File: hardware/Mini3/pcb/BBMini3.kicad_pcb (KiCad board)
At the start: 4 copper layers, 88 x 50 mm, 79 parts, among them J1 Conn_01x02, J2 USB_B_Mini, Q1 MBT2222ADW1T1, SW1 SW_SPDT, SW2 SW_Push, SW3 SW_Push, SW4 SW_Push, U1 ESP8266EX, U2 AT25SF081-SSHF-X, U3 AP2112K-3.3, U4 CP2104, U5 MCP3208, U6 LM2576S-5, U7 HD44780, U8 74HC595, Y1 ABM8-26.000MHZ-10-1-U-T

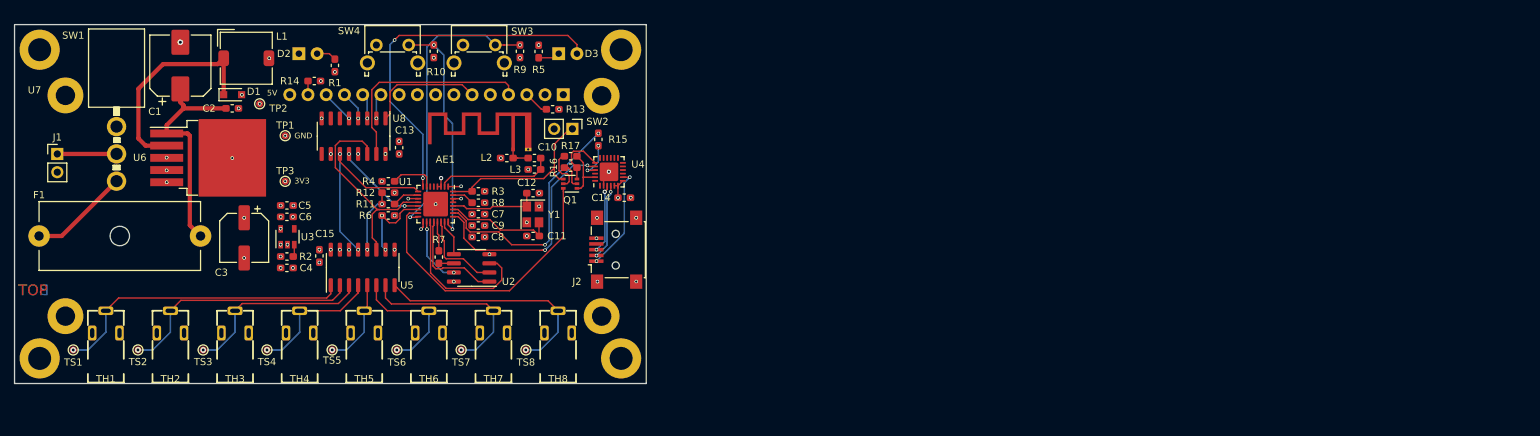
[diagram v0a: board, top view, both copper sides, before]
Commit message: feat: Version 3: Experimental PCB with only one ADC and multiplexer
shrink stuff, start pcb

Issue #24
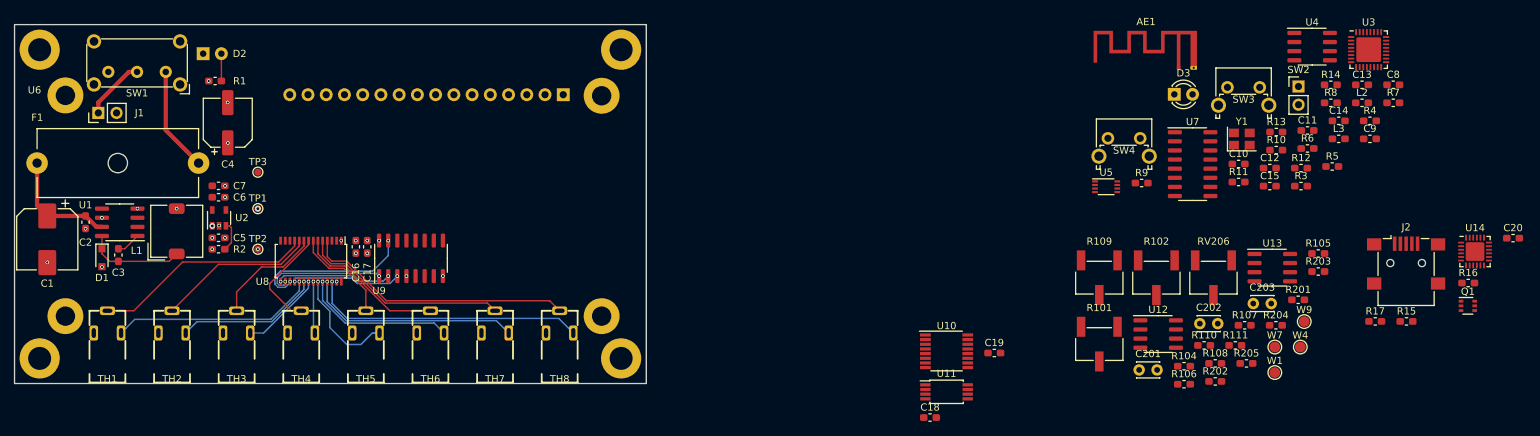
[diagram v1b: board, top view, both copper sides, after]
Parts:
- removed TS1, TS2, TS3, TS4, TS5, TS6, TS7, TS8: TestPoint, TestPoint:TestPoint_Pad_D1.0mm
- removed the U6 at (42.0, 33.6)
- added C16: 100n, Capacitor_SMD:C_0603_1608Metric_Pad1.05x0.95mm_HandSolder, F.Cu at (62.5, 46.0)
- added C17: 100n, Capacitor_SMD:C_0603_1608Metric_Pad1.05x0.95mm_HandSolder, F.Cu at (64.1, 46.0)
- added C18: 100n, Capacitor_SMD:C_0603_1608Metric_Pad1.05x0.95mm_HandSolder, F.Cu at (142.5, 69.7)
- added C19: 100n, Capacitor_SMD:C_0603_1608Metric_Pad1.05x0.95mm_HandSolder, F.Cu at (151.5, 60.7)
- added C20: 100n, Capacitor_SMD:C_0603_1608Metric_Pad1.05x0.95mm_HandSolder, F.Cu at (223.8, 44.7)
- added C201: 100n, Capacitor_THT:C_Disc_D3.0mm_W2.0mm_P2.50mm, F.Cu at (171.7, 63.1)
- added C202: 100n, Capacitor_THT:C_Disc_D3.0mm_W2.0mm_P2.50mm, F.Cu at (180.1, 56.7)
- added C203: 100n, Capacitor_THT:C_Disc_D3.0mm_W2.0mm_P2.50mm, F.Cu at (187.6, 53.9)
- added R101: 405, Potentiometer_SMD:Potentiometer_Bourns_3269W_Vertical, F.Cu at (166.1, 59.5)
- added R102: 300, Potentiometer_SMD:Potentiometer_Bourns_3269W_Vertical, F.Cu at (174.1, 50.3)
- added R104: 2k2, Resistor_SMD:R_0603_1608Metric_Pad1.05x0.95mm_HandSolder, F.Cu at (177.9, 62.6)
- added R105: 10k, Resistor_SMD:R_0603_1608Metric_Pad1.05x0.95mm_HandSolder, F.Cu at (196.6, 46.9)
- added R106: 10k, Resistor_SMD:R_0603_1608Metric_Pad1.05x0.95mm_HandSolder, F.Cu at (177.9, 65.1)
- added R107: 4k7, Resistor_SMD:R_0603_1608Metric_Pad1.05x0.95mm_HandSolder, F.Cu at (186.4, 56.9)
- added R108: 200, Resistor_SMD:R_0603_1608Metric_Pad1.05x0.95mm_HandSolder, F.Cu at (182.3, 62.2)
- added R109: 470, Potentiometer_SMD:Potentiometer_Bourns_3269W_Vertical, F.Cu at (166.1, 50.3)
- added R110: 200, Resistor_SMD:R_0603_1608Metric_Pad1.05x0.95mm_HandSolder, F.Cu at (180.7, 59.7)
- added R111: 2k, Resistor_SMD:R_0603_1608Metric_Pad1.05x0.95mm_HandSolder, F.Cu at (185.1, 59.7)
- added R201: 10k, Resistor_SMD:R_0603_1608Metric_Pad1.05x0.95mm_HandSolder, F.Cu at (193.8, 53.3)
- added R202: 10k, Resistor_SMD:R_0603_1608Metric_Pad1.05x0.95mm_HandSolder, F.Cu at (182.3, 64.7)
- added R203: 10k, Resistor_SMD:R_0603_1608Metric_Pad1.05x0.95mm_HandSolder, F.Cu at (196.6, 49.4)
- added R204: 100k, Resistor_SMD:R_0603_1608Metric_Pad1.05x0.95mm_HandSolder, F.Cu at (190.7, 56.9)
- added R205: 10k, Resistor_SMD:R_0603_1608Metric_Pad1.05x0.95mm_HandSolder, F.Cu at (186.6, 62.2)
- added RV206: 10k, Potentiometer_SMD:Potentiometer_Bourns_3269W_Vertical, F.Cu at (182.0, 50.3)
- added U10: ADG709, Package_SO:TSSOP-16_4.4x5mm_P0.65mm, F.Cu at (144.8, 60.5)
- added U11: MCP3202, Package_SO:TSSOP-8_4.4x3mm_P0.65mm, F.Cu at (144.8, 66.2)
- added U12: OPA2340, Package_SO:SOIC-8_3.9x4.9mm_P1.27mm, F.Cu at (174.3, 58.1)
- added U13: OPA2340, Package_SO:SOIC-8_3.9x4.9mm_P1.27mm, F.Cu at (190.2, 48.9)
- added U14: CP2104, Package_DFN_QFN:QFN-24-1EP_4x4mm_P0.5mm_EP2.6x2.6mm, F.Cu at (218.5, 46.6)
- added U7: 74HC595, Package_SO:SOIC-16_3.9x9.9mm_P1.27mm, F.Cu at (179.1, 34.4)
- added U9: 74HC595, Package_SO:SOIC-16_3.9x9.9mm_P1.27mm, F.Cu at (70.2, 47.6)
- added W1: ~, TestPoint:TestPoint_Pad_D1.5mm, F.Cu at (190.6, 63.5)
- added W4: ~, TestPoint:TestPoint_Pad_D1.5mm, F.Cu at (194.1, 59.9)
- added W7: ~, TestPoint:TestPoint_Pad_D1.5mm, F.Cu at (190.6, 59.9)
- added W9: ~, TestPoint:TestPoint_Pad_D1.5mm, F.Cu at (194.7, 56.4)
- C10: value 5p6 -> 100n
- C11: value 10p -> 5p6
- C13: value 100n -> 10p
- C3: value 100u -> 10n; footprint Capacitor_SMD:CP_Elec_6.3x5.9 -> Capacitor_SMD:C_0603_1608Metric_Pad1.05x0.95mm_HandSolder
- C4: value 10u -> 68u; footprint Capacitor_SMD:C_0603_1608Metric_Pad1.05x0.95mm_HandSolder -> Capacitor_SMD:CP_Elec_6.3x5.9
- C6: value 1u -> 10u
- C7: value 100n -> 1u
- D3: moved to F.Cu
- L1: value 100u -> 47u
- SW1: footprint Collection:MIYAMA_MS-500-B-VT -> Button_Switch_THT:SW_E-Switch_EG1224_SPDT_Angled
- U1: value ESP8266EX -> LM2672M-5.0; footprint Package_DFN_QFN:QFN-32-1EP_5x5mm_P0.5mm_EP3.45x3.45mm -> Package_SO:SOIC-8_3.9x4.9mm_P1.27mm
- U2: value AT25SF081-SSHF-X -> AP2112K-3.3; footprint Package_SO:SOIC-8_3.9x4.9mm_P1.27mm -> Package_TO_SOT_SMD:SOT-23-5
- U3: value AP2112K-3.3 -> ESP8266EX; footprint Package_TO_SOT_SMD:SOT-23-5 -> Package_DFN_QFN:QFN-32-1EP_5x5mm_P0.5mm_EP3.45x3.45mm
- U4: value CP2104 -> AT25SF081-SSHF-X; footprint Package_DFN_QFN:QFN-24-1EP_4x4mm_P0.5mm_EP2.6x2.6mm -> Package_SO:SOIC-8_3.9x4.9mm_P1.27mm
- U5: value MCP3208 -> SN74LVC1G139; footprint Package_SO:SOIC-16_3.9x9.9mm_P1.27mm -> Package_SO:VSSOP-8_2.3x2mm_P0.5mm
- U8: value 74HC595 -> ADG707; footprint Package_SO:SOIC-16_3.9x9.9mm_P1.27mm -> Package_SO:TSSOP-28_4.4x9.7mm_P0.65mm
- moved U3 152.9 mm to (203.6, 18.5), turned to 0 degrees
- moved R14 141.6 mm to (198.4, 23.4), turned to 0 degrees
- moved R4 137.0 mm to (203.8, 28.4), turned to 0 degrees
- moved R7 134.7 mm to (207.1, 25.9), turned to 0 degrees
- moved C13 134.4 mm to (202.7, 23.4), turned to 0 degrees
- moved C15 132.8 mm to (189.9, 37.5), turned to 0 degrees
- moved C8 129.2 mm to (207.1, 23.4), turned to 0 degrees
- moved R6 128.4 mm to (195.1, 32.3)
- moved R12 127.2 mm to (194.2, 35.0), turned to 0 degrees
- moved Q1 126.2 mm to (217.5, 54.2), turned to 0 degrees
- moved R16 126.1 mm to (217.5, 51.0), turned to 0 degrees
- moved C9 124.8 mm to (203.8, 30.9), turned to 0 degrees
- moved R8 119.6 mm to (198.4, 25.9)
- moved L2 119.4 mm to (202.7, 25.9), turned to 0 degrees
- moved R11 118.5 mm to (185.5, 36.9)
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- renumbered U7 to U6
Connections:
- C10 pad 1: Net-(AE1-Pad1) -> GND
- C10 pad 2: /ESP8266EX/LNA -> +3V3
- C11 pad 1: GND -> Net-(AE1-Pad1)
- C11 pad 2: /ESP8266EX/XTAL_OUT -> /ESP8266EX/LNA
- C12 pad 2: /ESP8266EX/XTAL_IN -> /ESP8266EX/XTAL_OUT
- C13 pad 1: +5V -> GND
- C13 pad 2: GND -> /ESP8266EX/XTAL_IN
- C14 pad 1: +3V3 -> +5V
- C15 pad 2: +5V -> +3V3
- C3 pad 1: +5V -> Net-(C3-Pad1)
- C3 pad 2: GND -> Net-(C3-Pad2)
- C4 pad 1: GND -> +5V
- C4 pad 2: +5V -> GND
- C5 pad 2: +3V3 -> +5V
- C7 pad 1: +3V3 -> GND
- C7 pad 2: GND -> +3V3
- C8 pad 1: GND -> +3V3
- C8 pad 2: +3V3 -> GND
- D1 pad 1: Net-(D1-Pad1) -> Net-(C3-Pad1)
- L1 pad 1: Net-(D1-Pad1) -> Net-(C3-Pad1)
- R6 pad 1: /ESP8266EX/CS1 -> /ESP8266EX/GPIO2
- TH1 pad R: +5V -> /Temperature/S1A
- TH1 pad S: GND -> +5V
- TH1 pad T: /Temperature/SIGNAL1 -> /Temperature/S1B
- TH2 pad R: +5V -> /Temperature/S2A
- TH2 pad S: GND -> +5V
- TH2 pad T: /Temperature/SIGNAL2 -> /Temperature/S2B
- TH3 pad R: +5V -> /Temperature/S3A
- TH3 pad S: GND -> +5V
- TH3 pad T: /Temperature/SIGNAL3 -> /Temperature/S3B
- TH4 pad R: +5V -> /Temperature/S4A
- TH4 pad S: GND -> +5V
- TH4 pad T: /Temperature/SIGNAL4 -> /Temperature/S4B
- TH5 pad R: +5V -> /Temperature/S5A
- TH5 pad S: GND -> +5V
- TH5 pad T: /Temperature/SIGNAL5 -> /Temperature/S5B
- TH6 pad R: +5V -> /Temperature/S6A
- TH6 pad S: GND -> +5V
- TH6 pad T: /Temperature/SIGNAL6 -> /Temperature/S6B
- TH7 pad R: +5V -> /Temperature/S7A
- TH7 pad S: GND -> +5V
- TH7 pad T: /Temperature/SIGNAL7 -> /Temperature/S7B
- TH8 pad R: +5V -> /Temperature/S8A
- TH8 pad S: GND -> +5V
- TH8 pad T: /Temperature/SIGNAL8 -> /Temperature/S8B
- U1 pad 1: +3V3 -> Net-(C3-Pad2)
- U1 pad 2: /ESP8266EX/LNA -> Net-(U1-Pad2)
- U1 pad 3: +3V3 -> Net-(U1-Pad3)
- U1 pad 4: +3V3 -> +5V
- U1 pad 6: /ESP8266EX/ADC -> GND
- U1 pad 7: /ESP8266EX/EN -> Net-(C1-Pad1)
- U1 pad 8: /ESP8266EX/GPIO16 -> Net-(C3-Pad1)
- U2 pad 1: /ESP8266EX/SDIO_CMD -> +5V
- U2 pad 2: /ESP8266EX/SDIO_DATA_0 -> GND
- U2 pad 3: /ESP8266EX/SDIO_DATA_3 -> Net-(R2-Pad1)
- U2 pad 4: GND -> Net-(U2-Pad4)
- U2 pad 5: /ESP8266EX/SDIO_DATA_1 -> +3V3
- U3 pad 1: +5V -> +3V3
- U3 pad 2: GND -> /ESP8266EX/LNA
- U3 pad 3: Net-(R2-Pad1) -> +3V3
- U3 pad 4: Net-(U3-Pad4) -> +3V3
- U3 pad 5: +3V3 -> Net-(U3-Pad5)
- U4 pad 1: Net-(U4-Pad1) -> /ESP8266EX/SDIO_CMD
- U4 pad 2: GND -> /ESP8266EX/SDIO_DATA_0
- U4 pad 3: Net-(J2-Pad3) -> /ESP8266EX/SDIO_DATA_3
- U4 pad 4: Net-(J2-Pad2) -> GND
- U4 pad 5: +3V3 -> /ESP8266EX/SDIO_DATA_1
- U4 pad 6: +3V3 -> Net-(R7-Pad1)
- U4 pad 7: +3V3 -> /ESP8266EX/SDIO_DATA_2
- U4 pad 8: Net-(J2-Pad1) -> +3V3
- U5 pad 1: /Temperature/SIGNAL1 -> /ESP8266EX/GPIO2
- U5 pad 2: /Temperature/SIGNAL2 -> /ESP8266EX/GPIO15
- U5 pad 3: /Temperature/SIGNAL3 -> Net-(U5-Pad3)
- U5 pad 4: /Temperature/SIGNAL4 -> GND
- U5 pad 5: /Temperature/SIGNAL5 -> /ESP8266EX/CS2
- U5 pad 6: /Temperature/SIGNAL6 -> /ESP8266EX/CS1
- U5 pad 7: /Temperature/SIGNAL7 -> CS0
- U5 pad 8: /Temperature/SIGNAL8 -> +3V3
- U8 pad 1: /ESP8266EX/ENABLE -> +5V
- U8 pad 10: +5V -> /Temperature/S2B
- U8 pad 11: /ESP8266EX/SCLK -> /Temperature/S1B
- U8 pad 12: /ESP8266EX/GPIO15 -> GND
- U8 pad 13: GND -> Net-(U8-Pad13)
- U8 pad 14: /ESP8266EX/MOSI -> Net-(U8-Pad14)
- U8 pad 15: /ESP8266EX/RS -> Net-(U8-Pad15)
- U8 pad 16: +5V -> Net-(U8-Pad16)
- U8 pad 2: /ESP8266EX/DB4 -> /Temperature/DB
- U8 pad 3: /ESP8266EX/DB5 -> Net-(U8-Pad3)
- U8 pad 4: /ESP8266EX/DB6 -> /Temperature/S8B
- U8 pad 5: /ESP8266EX/DB7 -> /Temperature/S7B
- U8 pad 6: Net-(U8-Pad6) -> /Temperature/S6B
- U8 pad 7: Net-(U8-Pad7) -> /Temperature/S5B
- U8 pad 8: GND -> /Temperature/S4B
- U8 pad 9: Net-(U8-Pad9) -> /Temperature/S3B
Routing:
- net /ESP8266EX/GPIO16: track 50.1 -> 0.00 mm, vias 2 -> 0
- net /Temperature/SIGNAL1: track 42.1 -> 0.00 mm, vias 1 -> 0
- net /ESP8266EX/GPIO0: track 40.8 -> 0.00 mm
- net /ESP8266EX/GPIO4: track 40.0 -> 0.00 mm, vias 2 -> 0
- net /Temperature/S8A: track 0.00 -> 38.3 mm, vias 0 -> 1
- net /Temperature/S8B: track 0.00 -> 37.7 mm
- net /Temperature/SIGNAL2: track 34.2 -> 0.00 mm, vias 1 -> 0
- net /ESP8266EX/GPIO3_RXD: track 33.8 -> 0.00 mm, vias 2 -> 0
- net /Temperature/SIGNAL8: track 32.7 -> 0.00 mm, vias 1 -> 0
- net /ESP8266EX/GPIO1_TXD: track 32.6 -> 0.00 mm, vias 2 -> 0
- net /ESP8266EX/GPIO5: track 31.5 -> 0.00 mm, vias 2 -> 0
- net /Temperature/S1B: track 0.00 -> 30.6 mm
- net /ESP8266EX/RS: track 30.1 -> 0.00 mm
- net /ESP8266EX/MOSI: track 30.1 -> 0.00 mm
- net Net-(D1-Pad1): track 30.0 -> 0.00 mm
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- removed copper zone on In1.Cu, net +3V3
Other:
- board text removed: "3V3"
- board text removed: "5V"
- board text removed: "BOT"
- board text removed: "GND"
- board text removed: "TOP"

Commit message: feat: Version 3: Experimental PCB with only one ADC and multiplexer
* add new PCB

Issue #24
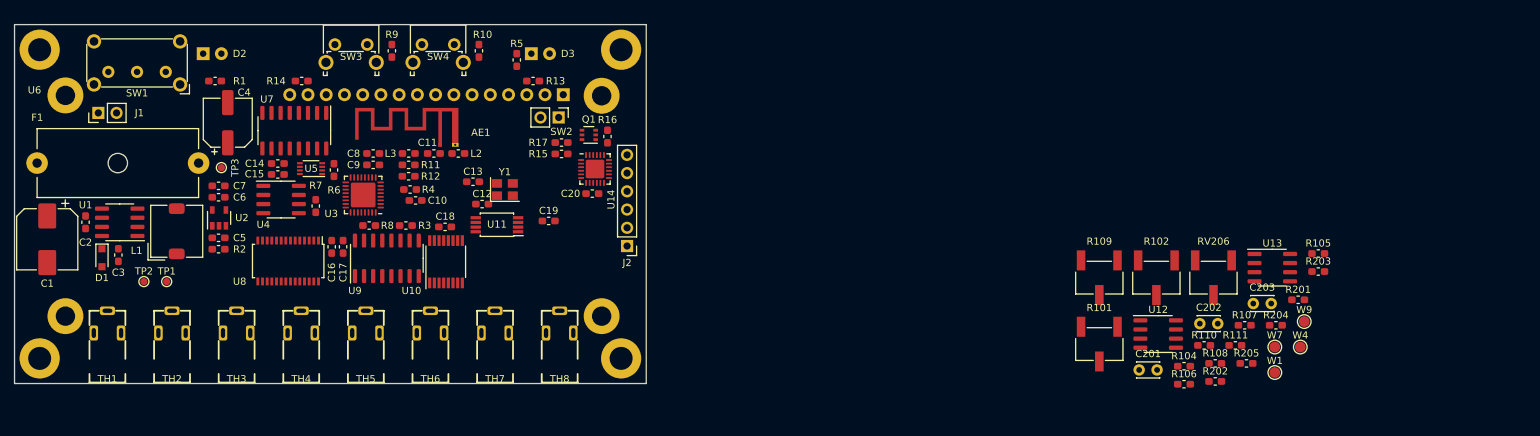
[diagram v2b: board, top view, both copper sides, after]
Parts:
- D3: moved to B.Cu
- J2: footprint Connector_USB:USB_Mini-B_Lumberg_2486_01_Horizontal -> Connector_PinHeader_2.54mm:PinHeader_1x06_P2.54mm_Vertical
- moved R7 150.8 mm to (57.0, 40.3), turned to 270 degrees
- moved C14 147.9 mm to (51.7, 34.4)
- moved U4 145.2 mm to (52.1, 39.4)
- moved R14 143.4 mm to (55.0, 22.9)
- moved C8 142.4 mm to (65.0, 33.0)
- moved U3 141.5 mm to (63.6, 38.7), turned to 180 degrees
- moved C9 138.9 mm to (65.0, 34.5), turned to 180 degrees
- moved C15 138.2 mm to (51.7, 35.9)
- moved R6 135.6 mm to (59.5, 35.3), turned to 90 degrees
- moved R8 135.0 mm to (64.4, 43.0), turned to 180 degrees
- moved R4 134.1 mm to (70.1, 38.0)
- moved L3 129.6 mm to (69.9, 33.0), turned to 180 degrees
- moved C20 128.4 mm to (95.5, 38.5)
- moved L2 126.1 mm to (76.8, 33.0)
- moved U7 125.2 mm to (54.0, 29.8), turned to 270 degrees
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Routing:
- net /Temperature/S8A: track 38.3 -> 0.00 mm, vias 1 -> 0
- net /Temperature/S8B: track 37.7 -> 0.00 mm
- net /Temperature/S1B: track 30.6 -> 0.00 mm
- net /Temperature/S7A: track 29.9 -> 0.00 mm, vias 1 -> 0
- net /Temperature/S7B: track 29.3 -> 0.00 mm
- net /Temperature/S1A: track 28.5 -> 0.00 mm, vias 1 -> 0
- net Net-(U8-Pad17): track 22.9 -> 0.00 mm, vias 2 -> 0
- net /Temperature/S2B: track 22.2 -> 0.00 mm
- net /Temperature/S6A: track 21.4 -> 0.00 mm, vias 1 -> 0
- net /Temperature/S6B: track 20.8 -> 0.00 mm
- net /Temperature/S2A: track 20.1 -> 0.00 mm, vias 1 -> 0
- net Net-(U8-Pad16): track 17.0 -> 0.00 mm, vias 2 -> 0
- net Net-(C1-Pad1): track 16.2 -> 0.00 mm
- net Net-(U8-Pad15): track 16.1 -> 0.00 mm, vias 2 -> 0
- net /Temperature/S5A: track 15.6 -> 0.00 mm, vias 1 -> 0
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
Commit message: feat: Version 3: Experimental PCB with only one ADC and multiplexer
more work on pcb

Issue #24
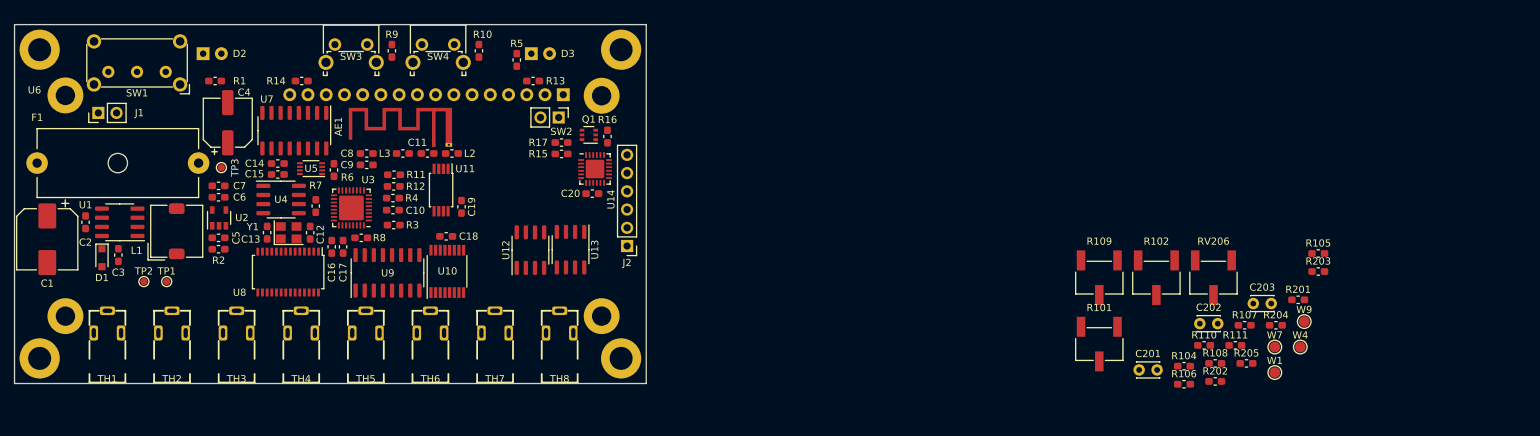
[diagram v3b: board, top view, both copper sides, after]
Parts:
- moved U13 97.8 mm to (92.5, 46.4), turned to 270 degrees
- moved U12 88.2 mm to (86.9, 46.4), turned to 90 degrees
- moved Y1 30.7 mm to (53.2, 44.0)
- moved C13 29.5 mm to (50.2, 44.0), turned to 270 degrees
- moved C12 24.3 mm to (56.2, 44.0), turned to 90 degrees
- moved C19 12.3 mm to (77.3, 40.4), turned to 270 degrees
- moved U11 9.16 mm to (74.4, 38.0), turned to 270 degrees
- moved C10 3.43 mm to (67.7, 40.8)
- moved R4 2.67 mm to (67.7, 39.2)
- moved R12 2.51 mm to (67.8, 37.5)
- moved R11 2.45 mm to (67.9, 35.9)
- moved U3 2.44 mm to (61.9, 40.5)
- moved R8 2.04 mm to (63.3, 44.7)
- moved U9 2.02 mm to (67.0, 49.6)
- moved R3 1.70 mm to (67.8, 42.9)
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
